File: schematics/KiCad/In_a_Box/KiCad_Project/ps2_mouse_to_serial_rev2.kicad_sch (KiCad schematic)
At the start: 24 parts, among them J1 Barrel Jack 2.1 mm, J2 DB9 Female, J3 Mini-DIN-6, Q1 BC547, SW1 1C2P, U1 74LS00, U2 L7805, U3 L78L05

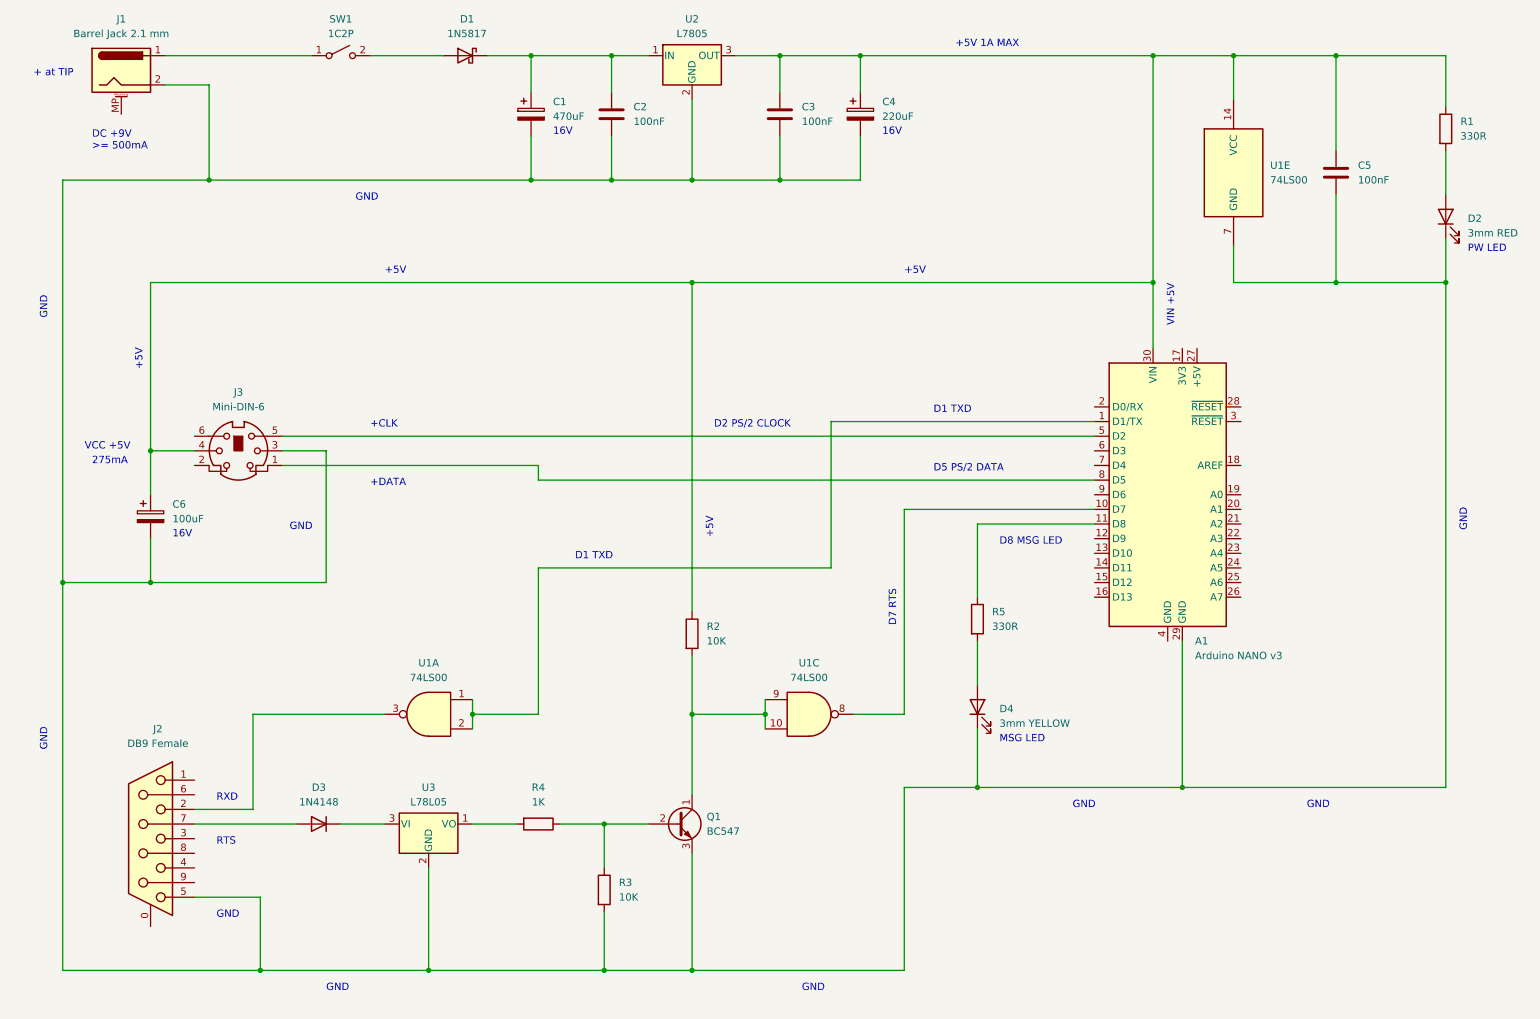
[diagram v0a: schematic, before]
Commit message: v1.0.1-rev2
- Se añade el esquema realizado en formato KiCad.
- Corregido un error en la conexión a masa del condensador C6 en el esquema en formato TinyCad.
- Modificadas algunas de las anotaciones en los pins de Arduino en el esquema en formato TinyCad.
- Añadidos los esquemas de KiCad en formato PDF y PNG.
- Añadidos los diseños de las PBC para las version "Stand Alone" y "In-a-Box". Estos diseños se han mandado a producción, pero aún no se han verificado.
- No hay cambios en el código.
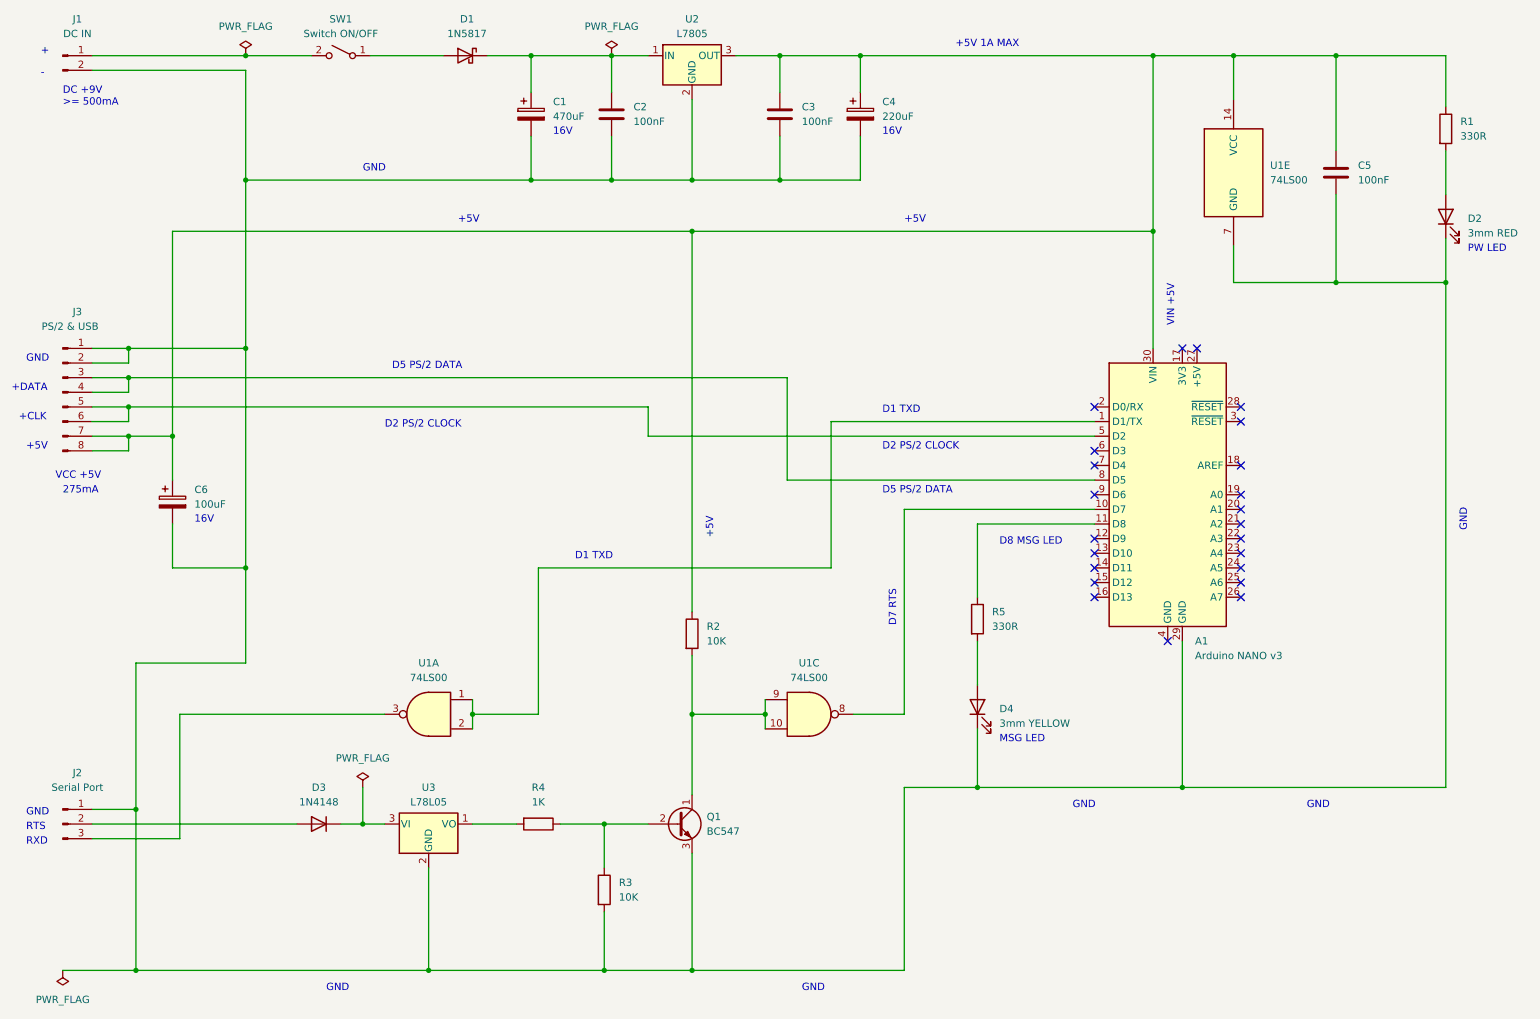
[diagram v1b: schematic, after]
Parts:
- removed J1: Barrel Jack 2.1 mm, Connector_BarrelJack:BarrelJack_CUI_PJ-063AH_Horizontal, symbol Connector:Barrel_Jack_MountingPin
- removed J2: DB9 Female, symbol Connector:DE9_Receptacle_MountingHoles
- removed J3: Mini-DIN-6, symbol Connector:Mini-DIN-6
- added J1: DC IN, TerminalBlock_TE-Connectivity:TerminalBlock_TE_282834-2_1x02_P2.54mm_Horizontal, symbol Connector:Conn_01x02_Pin
- added J2: Serial Port, TerminalBlock_TE-Connectivity:TerminalBlock_TE_282834-3_1x03_P2.54mm_Horizontal, symbol Connector:Conn_01x03_Pin
- added J3: PS/2 & USB, Connector_PinHeader_2.54mm:PinHeader_2x04_P2.54mm_Vertical, symbol Connector:Conn_01x08_Pin
- D2, D4: footprint (none) -> LED_THT:LED_D3.0mm
- SW1: value 1C2P -> Switch ON/OFF; footprint (none) -> TerminalBlock_TE-Connectivity:TerminalBlock_TE_282834-2_1x02_P2.54mm_Horizontal
- U1: footprint (none) -> Package_DIP:DIP-14_W7.62mm_Socket
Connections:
- net at A1.30 (VIN), C3.1, C4.1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: now also J3.7 (Pin_7), J3.8 (Pin_8)
- net at A1.29 (GND), C1.2, C2.2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: now also J1.2 (Pin_2), J2.1 (Pin_1), J3.1 (Pin_1), J3.2 (Pin_2)
- net at D1.2 (A): now also SW1.1 (A); no longer SW1.2 (B)
- net at A1.5 (D2): now also J3.5 (Pin_5), J3.6 (Pin_6)
- net at A1.8 (D5): now also J3.3 (Pin_3), J3.4 (Pin_4)
- net at D3.2 (A): now also J2.2 (Pin_2)
- net at U1.3: now also J2.3 (Pin_3)
- new net: J1.1 (Pin_1), SW1.2 (B)
- no-connect marks 0 -> 23
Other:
- note added: "+"
- note added: "-"
- note removed: "+ at TIP"
- moved on the sheet: C6
